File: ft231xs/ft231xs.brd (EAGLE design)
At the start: 100 x 100 mm, 23 parts, among them U3 AP2112K-3.3V

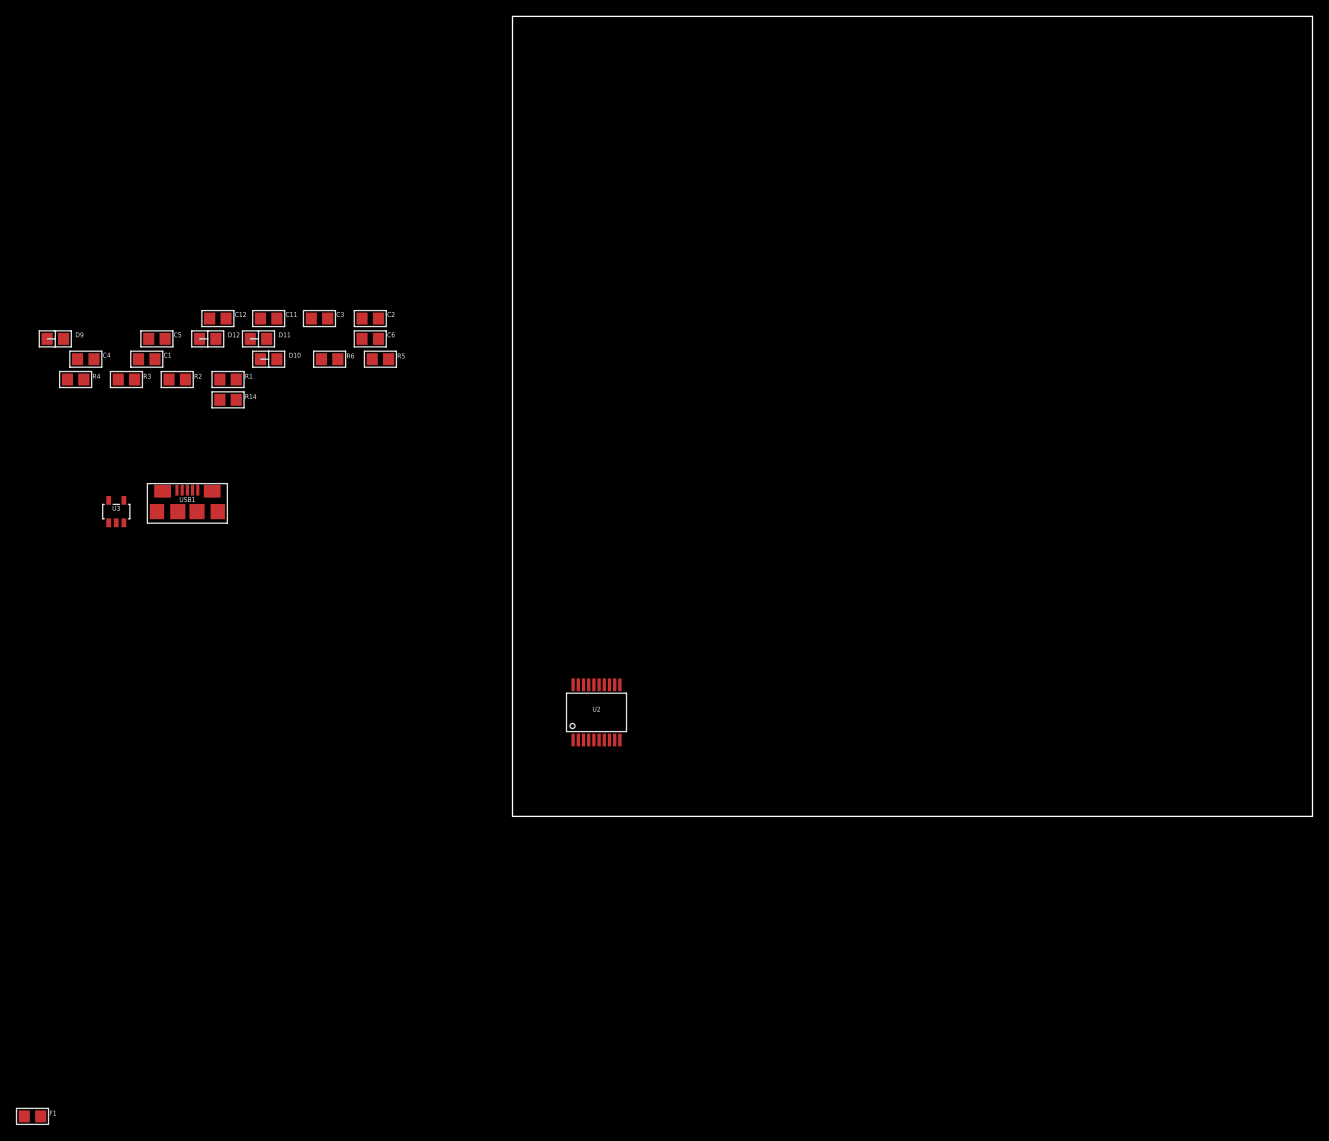
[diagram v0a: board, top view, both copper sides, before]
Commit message: add 232 module and finish the ft231
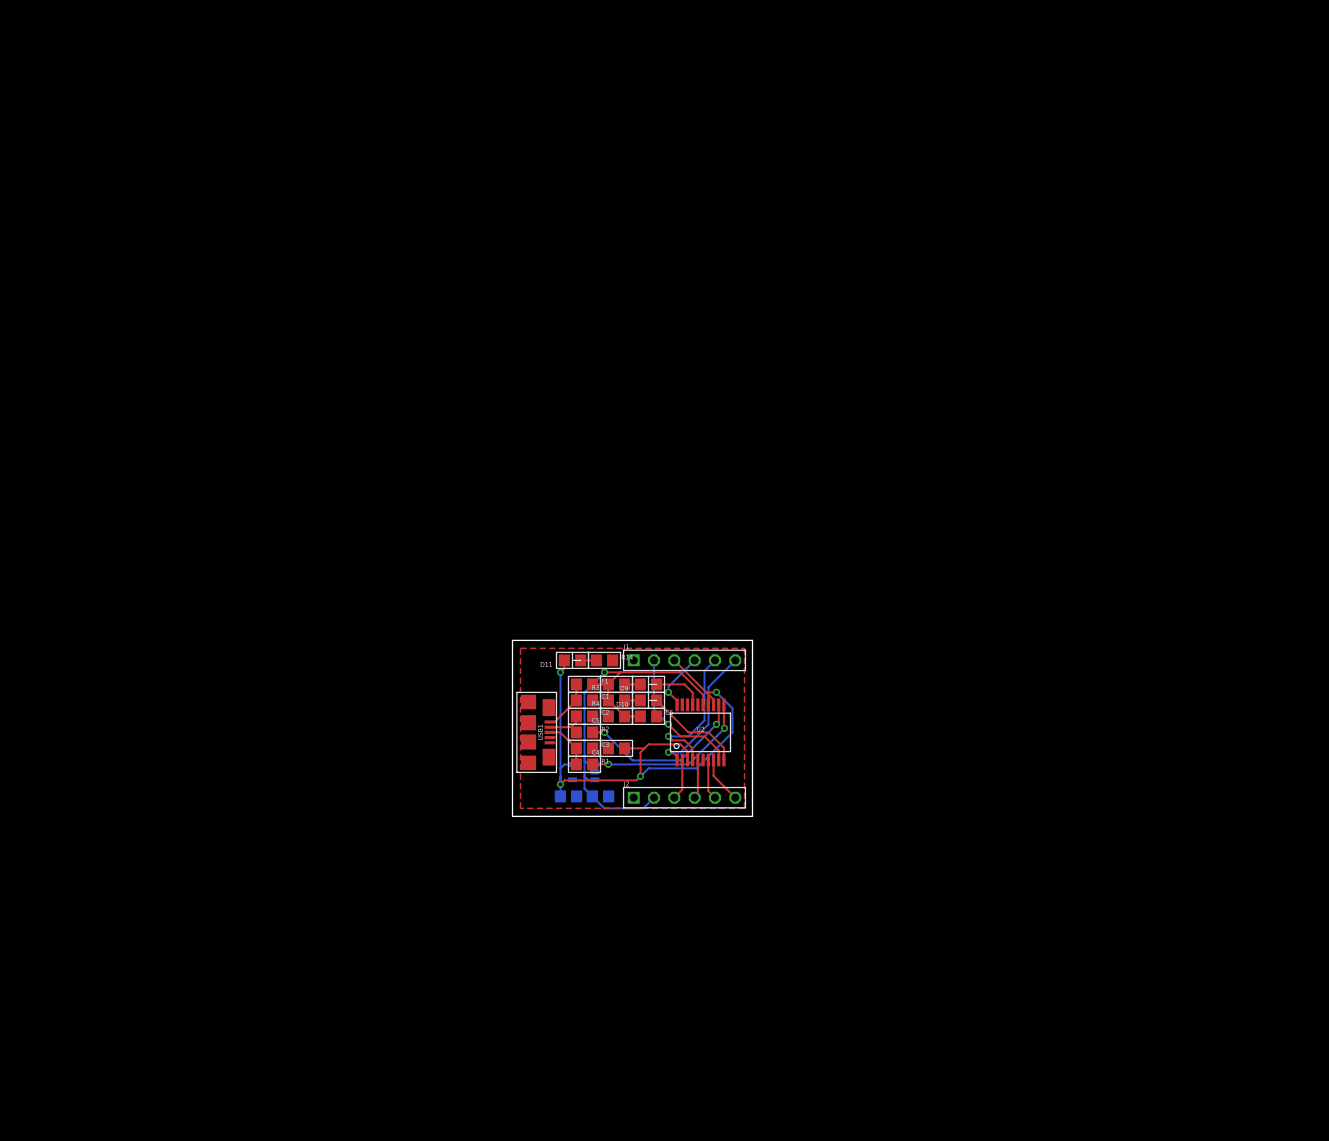
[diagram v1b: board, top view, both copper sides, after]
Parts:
- removed D12: (no value), Diodes:0805DIODE
- removed R5, R6: 1K, Resistors:0805
- added J1, J2: (no value), Connectors:6PIN_HEADER_PITCH2.54MM_TH
- moved F1 87.6 mm to (9.00, 16.5)
- moved D9 85.8 mm to (17.0, 16.5), turned to 180 degrees
- moved C4 82.3 mm to (13.0, 8.50), turned to 180 degrees
- moved R4 78.6 mm to (13.0, 14.5), turned to 180 degrees
- moved C5 74.3 mm to (13.0, 12.5), turned to 180 degrees
- moved C12 74.1 mm to (7.00, 2.50), flipped to the bottom, turned to 180 degrees
- moved C11 72.7 mm to (11.0, 2.50), flipped to the bottom, turned to 180 degrees
- moved R3 72.1 mm to (13.0, 16.5), turned to 180 degrees
- moved C1 69.4 mm to (9.00, 14.5)
- moved R2 67.4 mm to (9.00, 10.5)
- moved U3 66.9 mm to (8.90, 5.53), flipped to the bottom, turned to 270 degrees
- moved R1 65.6 mm to (9.00, 6.50)
- moved D10 63.8 mm to (17.0, 14.5), turned to 180 degrees
- moved C3 63.1 mm to (9.00, 8.50)
- moved C6 58.6 mm to (17.0, 12.5)
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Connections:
- removed net 3.3V_: C4.1, U2.13, U2.14, U2.3
- removed net RXI: R6.2
- removed net TXO: R5.2
- removed net USBVCC: C5.1, C6.1, D12.2, F1.2, R3.2, R4.2, U2.15
- net +3V3: now also C4.1, J1.3, U2.13, U2.14, U2.3
- net +5V: now also C5.1, C6.1, F1.2, J2.2, R3.2, R4.2, U2.15; no longer D12.1
- net CTS: now also J1.2
- net DCD: now also J2.6
- net DGND: now also J1.1, J2.1
- net DSR: now also J2.5
- net DTR: now also J1.6
- net RI: now also J2.4
- net RTS: now also J2.3
- net RXD: now also J1.5; no longer R5.1
- net TXD: now also J1.4; no longer R6.1
- net VBUS: now also USB1.1
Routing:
- net +3V3: track 0.00 -> 73.3 mm, vias 0 -> 4
- net +5V: track 0.00 -> 54.4 mm, vias 0 -> 1
- net N$27: track 0.00 -> 21.4 mm, vias 0 -> 2
- net N$28: track 0.00 -> 21.3 mm, vias 0 -> 2
- net RXD: track 0.00 -> 18.5 mm, vias 0 -> 1
- net CTS: track 0.00 -> 17.6 mm, vias 0 -> 1
- net DTR: track 0.00 -> 17.5 mm, vias 0 -> 1
- net TX_LED: track 0.00 -> 12.4 mm
- net TXD: track 0.00 -> 7.35 mm, vias 0 -> 1
- net RX_LED: track 0.00 -> 6.45 mm
- net VBUS: track 0.00 -> 6.42 mm
- net D+: track 0.00 -> 6.13 mm
- net DCD: track 0.00 -> 5.84 mm
- net D-: track 0.00 -> 5.19 mm
- net RTS: track 0.00 -> 5.12 mm
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- added copper zone on layer 1, net DGND
- added copper zone on layer 16, net DGND
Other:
- board size 100 x 100 mm -> 30 x 22 mm

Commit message: the ft231xs is ready
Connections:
- net DGND: now also USB1.M1, USB1.M2, USB1.M3, USB1.M4
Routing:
- net +5V: track 54.4 -> 53.9 mm
- net +3V3: track 73.3 -> 72.8 mm
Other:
- outline, holes or cut-outs redrawn
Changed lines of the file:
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@@
 <?xml version="1.0" encoding="utf-8"?>
 <!DOCTYPE eagle SYSTEM "eagle.dtd">
-<eagle version="7.5.0">
+<eagle version="8.1.1">
 <drawing>
 <settings>
@@
 <layer number="2" name="Route2" color="1" fill="3" visible="yes" active="yes"/>
 <layer number="3" name="Route3" color="4" fill="3" visible="no" active="yes"/>
+<layer number="4" name="Route4" color="1" fill="4" visible="no" active="no"/>
+<layer number="5" name="Route5" color="4" fill="4" visible="no" active="no"/>
+<layer number="6" name="Route6" color="1" fill="8" visible="no" active="no"/>
+<layer number="7" name="Route7" color="4" fill="8" visible="no" active="no"/>
+<layer number="8" name="Route8" color="1" fill="2" visible="no" active="no"/>
+<layer number="9" name="Route9" color="4" fill="2" visible="no" active="no"/>
+<layer number="10" name="Route10" color="1" fill="7" visible="no" active="no"/>
+<layer number="11" name="Route11" color="4" fill="7" visible="no" active="no"/>
+<layer number="12" name="Route12" color="1" fill="5" visible="no" active="no"/>
+<layer number="13" name="Route13" color="4" fill="5" visible="no" active="no"/>
 <layer number="14" name="Route14" color="1" fill="6" visible="no" active="yes"/>
 <layer number="15" name="Route15" color="4" fill="6" visible="no" active="yes"/>
@@
 <board>
 <plain>
-<wire x1="0" y1="0" x2="30" y2="0" width="0.1" layer="20"/>
-<wire x1="30" y1="0" x2="30" y2="22" width="0.1" layer="20"/>
-<wire x1="30" y1="22" x2="0" y2="22" width="0.1" layer="20"/>
-<wire x1="0" y1="22" x2="0" y2="0" width="0.1" layer="20"/>
+<wire x1="0" y1="20" x2="0" y2="2" width="0.1" layer="20"/>
+<wire x1="0" y1="2" x2="2" y2="0" width="0.1" layer="20" curve="90"/>
+<wire x1="2" y1="0" x2="28" y2="0" width="0.1" layer="20"/>
+<wire x1="28" y1="0" x2="30" y2="2" width="0.1" layer="20" curve="90"/>
+<wire x1="30" y1="2" x2="30" y2="20" width="0.1" layer="20"/>
+<wire x1="30" y1="20" x2="28" y2="22" width="0.1" layer="20" curve="90"/>
+<wire x1="28" y1="22" x2="2" y2="22" width="0.1" layer="20"/>
+<wire x1="2" y1="22" x2="0" y2="20" width="0.1" layer="20" curve="90"/>
 </plain>
 <attributes>
@@
 <contactref element="C12" pad="2"/>
 <polygon width="0.254" layer="1">
-<vertex x="1" y="21"/>
-<vertex x="29" y="21"/>
-<vertex x="29" y="1"/>
-<vertex x="1" y="1"/>
+<vertex x="27" y="1"/>
+<vertex x="3" y="1" curve="-90"/>
+<vertex x="1" y="3"/>
+<vertex x="1" y="19" curve="-90"/>
+<vertex x="3" y="21"/>
+<vertex x="27" y="21" curve="-90"/>
+<vertex x="29" y="19"/>
+<vertex x="29" y="3" curve="-90"/>
 </polygon>
 <contactref element="J1" pad="1"/>
 <contactref element="J2" pad="1"/>
 <polygon width="0.254" layer="16">
-<vertex x="1" y="21"/>
-<vertex x="29" y="21"/>
-<vertex x="29" y="1"/>
-<vertex x="1" y="1"/>
+<vertex x="27" y="1"/>
+<vertex x="3" y="1" curve="-90"/>
+<vertex x="1" y="3"/>
+<vertex x="1" y="19" curve="-90"/>
+<vertex x="3" y="21"/>
+<vertex x="27" y="21" curve="-90"/>
+<vertex x="29" y="19"/>
+<vertex x="29" y="3" curve="-90"/>
 </polygon>
+<contactref element="USB1" pad="M1"/>
+<contactref element="USB1" pad="M2"/>
+<contactref element="USB1" pad="M3"/>
+<contactref element="USB1" pad="M4"/>
 </signal>
 <signal name="D+">
@@
 <wire x1="7.5" y1="6.48" x2="6.48" y2="6.48" width="0.254" layer="16"/>
 <wire x1="6.48" y1="6.48" x2="6" y2="6" width="0.254" layer="16"/>
-<via x="16" y="5" extent="1-16" drill="0.5"/>
-<wire x1="21" y1="9" x2="17" y2="9" width="0.254" layer="1"/>
-<wire x1="16.5" y1="8.5" x2="16" y2="8" width="0.254" layer="1"/>
-<wire x1="16" y1="8" x2="16" y2="5" width="0.254" layer="1"/>
-<wire x1="14.025" y1="8.5" x2="16.5" y2="8.5" width="0.254" layer="1"/>
-<wire x1="16.5" y1="8.5" x2="17" y2="9" width="0.254" layer="1"/>
+<via x="16.5" y="5.5" extent="1-16" drill="0.5"/>
+<wire x1="21" y1="9" x2="17.5" y2="9" width="0.254" layer="1"/>
+<wire x1="17" y1="8.5" x2="16.5" y2="8" width="0.254" layer="1"/>
+<wire x1="16.5" y1="8" x2="16.5" y2="5.5" width="0.254" layer="1"/>
+<wire x1="14.025" y1="8.5" x2="17" y2="8.5" width="0.254" layer="1"/>
+<wire x1="17" y1="8.5" x2="17.5" y2="9" width="0.254" layer="1"/>
 <wire x1="27.5" y1="10.5" x2="23" y2="6" width="0.254" layer="16"/>
 <wire x1="23" y1="6" x2="17" y2="6" width="0.254" layer="16"/>
@@
 <wire x1="25.5" y1="15.5" x2="27.5" y2="13.5" width="0.254" layer="16"/>
 <wire x1="27.5" y1="13.5" x2="27.5" y2="10.5" width="0.254" layer="16"/>
-<wire x1="16" y1="5" x2="15.5" y2="4.5" width="0.254" layer="1"/>
+<wire x1="16.5" y1="5.5" x2="15.5" y2="4.5" width="0.254" layer="1"/>
 <wire x1="15.5" y1="4.5" x2="6.5" y2="4.5" width="0.254" layer="1"/>
 <wire x1="6.5" y1="4.5" x2="6" y2="4" width="0.254" layer="1"/>
-<wire x1="17" y1="6" x2="16" y2="5" width="0.254" layer="16"/>
+<wire x1="17" y1="6" x2="16.5" y2="5.5" width="0.254" layer="16"/>
 </signal>
 <signal name="+5V">
@@
 <wire x1="13.475" y1="18" x2="11.975" y2="16.5" width="0.254" layer="1"/>
 <contactref element="J2" pad="2"/>
-<wire x1="11" y1="1.5" x2="11.5" y2="1" width="0.254" layer="16"/>
-<wire x1="11.5" y1="1" x2="16.35" y2="1" width="0.254" layer="16"/>
-<wire x1="16.35" y1="1" x2="17.69" y2="2.34" width="0.254" layer="16"/>
-<wire x1="11" y1="1.5" x2="10.975" y2="1.5" width="0.254" layer="16"/>
-<wire x1="10.975" y1="1.5" x2="9.975" y2="2.5" width="0.254" layer="16"/>
 <via x="11.5" y="18" extent="1-16" drill="0.5"/>
 <wire x1="11.5" y1="18" x2="13.475" y2="18" width="0.254" layer="1"/>
@@
 <wire x1="9" y1="7" x2="9" y2="15.5" width="0.254" layer="16"/>
 <wire x1="9" y1="15.5" x2="11.5" y2="18" width="0.254" layer="16"/>
-<wire x1="10.3" y1="4.58" x2="9.42" y2="4.58" width="0.254" layer="16"/>
+<wire x1="9.42" y1="4.58" x2="10.3" y2="4.58" width="0.254" layer="16"/>
 <wire x1="9.42" y1="4.58" x2="9" y2="5" width="0.254" layer="16"/>
 <wire x1="10.3" y1="6.48" x2="9.52" y2="6.48" width="0.254" layer="16"/>
 <wire x1="9.52" y1="6.48" x2="9" y2="7" width="0.254" layer="16"/>
+<wire x1="10.3" y1="4.58" x2="15.45" y2="4.58" width="0.254" layer="16"/>
+<wire x1="15.45" y1="4.58" x2="17.69" y2="2.34" width="0.254" layer="16"/>
 </signal>
 <signal name="N$35">
